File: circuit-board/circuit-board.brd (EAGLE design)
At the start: 100 x 80 mm, 51 parts, among them IC1 UA78M05DCY, Q1 BC547B, Q2 BC547B, U1 MAX3232, U2 ATMEGA328P_TQFP, U3 ADUM1201BRZ, Y2 16MHz

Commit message: Lay out circuit board, preliminary
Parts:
- removed 12V-IN-GPS: JST-XH-02-PIN-LONG-PAD, Rembrandt Electronics - JST XH Connectors v1-0:JST-XH-02-PACKAGE-LONG-PAD
- added 12V-IN: JST-XH-02-PIN-LONG-PAD, Rembrandt Electronics - JST XH Connectors v1-0:JST-XH-02-PACKAGE-LONG-PAD
- moved R10 74.6 mm to (39.4, 14.0), turned to 270 degrees
- moved Q2 51.3 mm to (44.5, 38.1)
- moved OK1 48.6 mm to (30.5, 11.4), turned to 270 degrees
- moved C5 45.1 mm to (35.6, 17.8), turned to 180 degrees
- moved C12 43.3 mm to (2.54, 5.08)
- moved EXP-GND 43.1 mm to (54.6, 38.1)
- moved EXT-GND 43.1 mm to (57.1, 38.1)
- moved HANDSET 43.1 mm to (50.8, 45.7)
- moved Y2 40.6 mm to (2.54, 8.89), turned to 270 degrees
- moved UC-DBG 40.4 mm to (5.08, 2.54), turned to 180 degrees
- moved MIC-XFMR 39.9 mm to (34.3, 27.9)
- moved C1 39.6 mm to (31.8, 38.1), turned to 90 degrees
- moved C13 38.6 mm to (2.54, 12.7), turned to 180 degrees
- moved SPK-SW 38.3 mm to (55.9, 14.0), turned to 0 degrees
- moved R1 38.1 mm to (58.4, 10.2)
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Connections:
- net 12V: now also 12V-IN.2; no longer 12V-IN-GPS.2
- net GNDA: now also 12V-IN.1; no longer 12V-IN-GPS.1
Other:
- board size 100 x 80 mm -> 61 x 50.8 mm

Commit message: Minimize V2 board layout
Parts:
- moved ICSP 33.5 mm to (2.03, 37.0)
- moved UC-DBG 23.6 mm to (2.03, 25.9), turned to 270 degrees
- moved R3 20.7 mm to (32.1, 7.62)
- moved UC-SS 16.0 mm to (14.5, 18.3), turned to 0 degrees
- moved 12V-IN 16.0 mm to (14.7, 34.3)
- moved FB1 14.9 mm to (10.5, 30.6)
- moved R6 14.7 mm to (14.0, 30.6)
- moved C18 14.5 mm to (17.4, 30.6)
- moved Q2 11.1 mm to (33.8, 35.2)
- moved C9 10.5 mm to (36.7, 9.27)
- moved R1 10.5 mm to (48.3, 7.49), turned to 180 degrees
- moved EXP-GND 10.5 mm to (44.6, 35.1)
- moved EXT-GND 10.5 mm to (47.1, 35.1)
- moved R7 10.4 mm to (26.7, 38.2)
- moved SPK-XFMR 10.3 mm to (42.0, 25.4)
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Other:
- board size 61 x 50.8 mm -> 50.8 x 45.7 mm

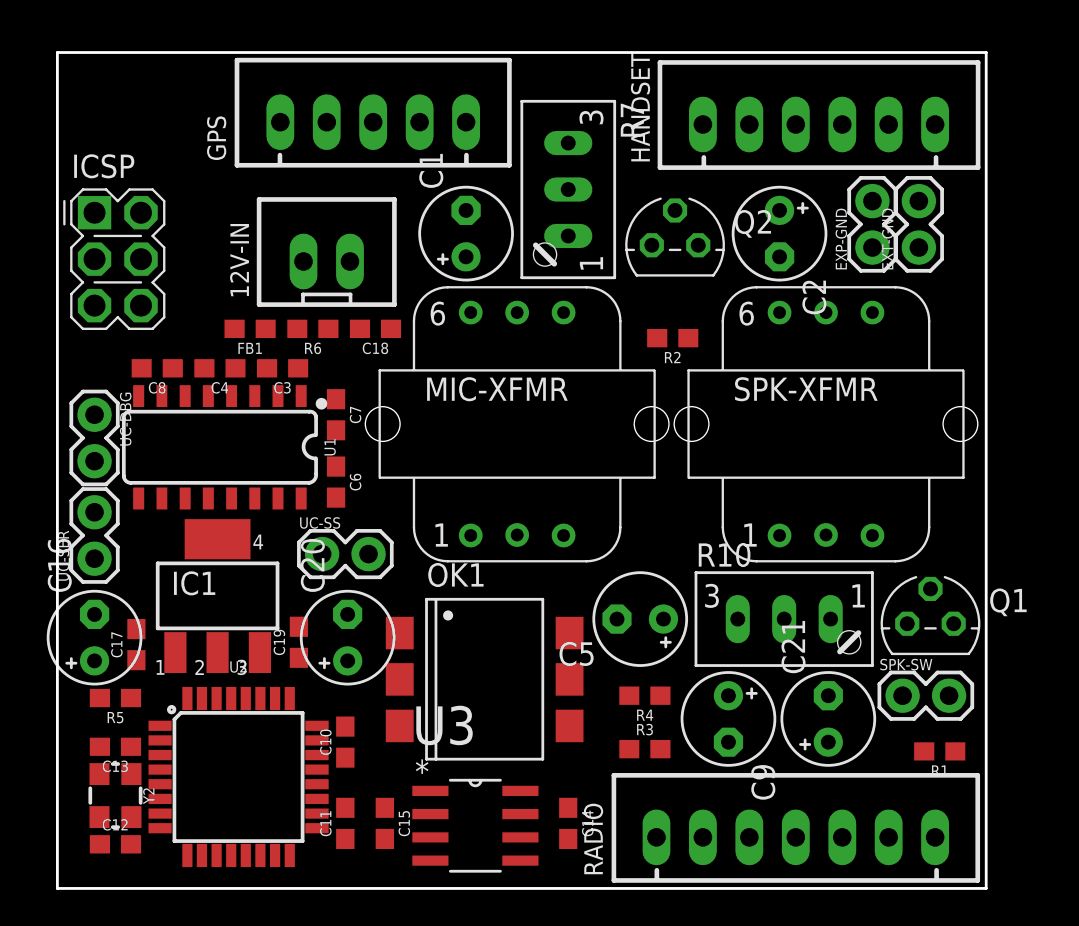
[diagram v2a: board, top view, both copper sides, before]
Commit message: Add ground planes, routes to V2 board
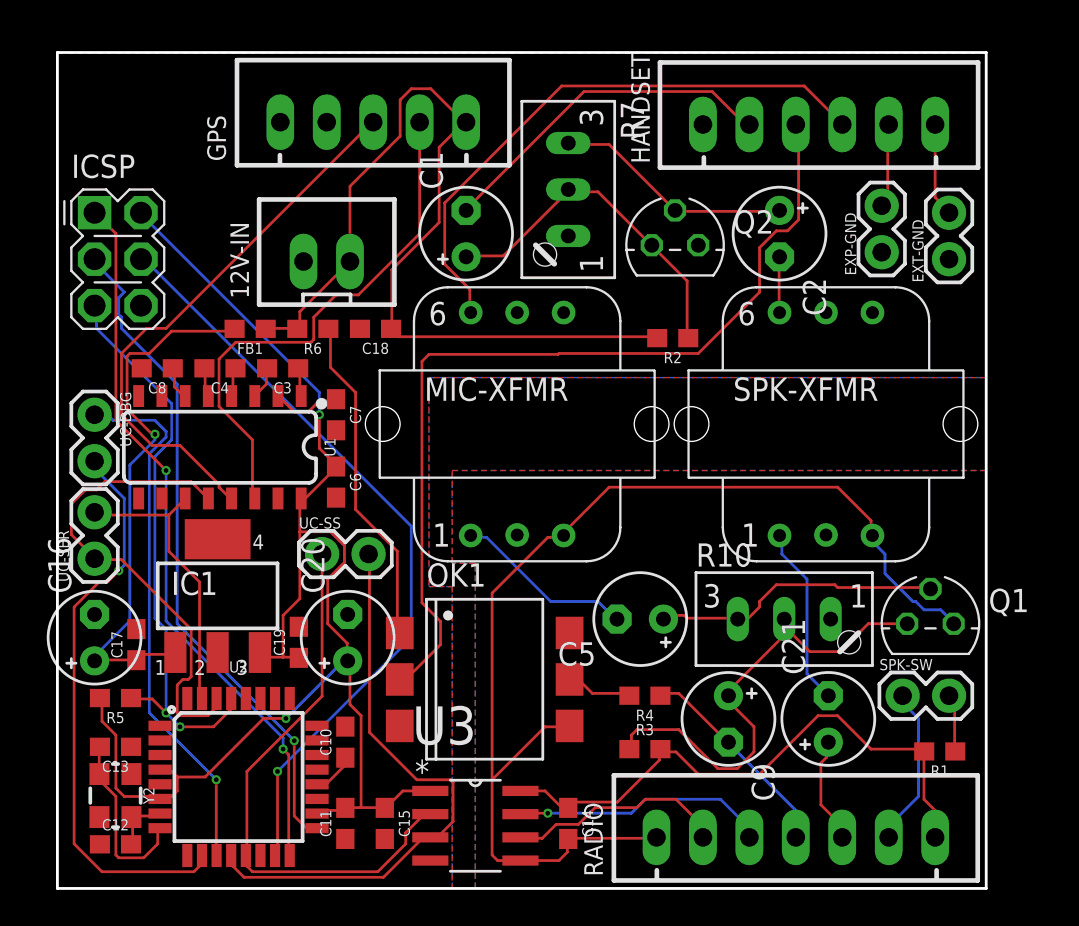
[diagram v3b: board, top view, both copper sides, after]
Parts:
- R10, R7: value (none) -> 100k
- moved EXT-GND 1.77 mm to (48.8, 34.4)
- moved EXP-GND 0.57 mm to (45.1, 34.8)
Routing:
- net +5V: track 0.00 -> 80.5 mm, vias 0 -> 2
- net GND: track 0.00 -> 62.1 mm
- net HANDSET-PTT: track 0.00 -> 49.9 mm
- net 12V: track 0.00 -> 49.1 mm
- net UC-MOSI: track 0.00 -> 42.1 mm, vias 0 -> 1
- net UC-MISO: track 0.00 -> 39.6 mm, vias 0 -> 2
- net UC-SCK: track 0.00 -> 36.8 mm, vias 0 -> 1
- net 3.3V: track 0.00 -> 32.0 mm
- net HANDSET-MIC: track 0.00 -> 31.9 mm
- net UC-SS-TX: track 0.00 -> 31.8 mm
- net UC-RESET: track 0.00 -> 31.8 mm, vias 0 -> 2
- net UC-DBG-TX: track 0.00 -> 31.3 mm, vias 0 -> 1
- net UC-SS-RX: track 0.00 -> 30.6 mm
- net GPS-TX: track 0.00 -> 30.4 mm
- net N$1: track 0.00 -> 29.9 mm, vias 0 -> 1
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- added copper zone on layer 1, net GND
- added copper zone on layer 16, net GND
- added copper zone on layer 1, net GNDA
- added copper zone on layer 16, net GNDA

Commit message: Route V2 board manually, fix up silkscreen
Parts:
- U2: value ATMEGA328P_TQFP -> ATMEGA328P
- moved ICSP 33.9 mm to (11.9, 4.57), turned to 270 degrees
- moved C16 28.0 mm to (4.32, 41.7), turned to 0 degrees
- moved C17 25.8 mm to (3.94, 39.1), turned to 0 degrees
- moved UC-DBG 24.0 mm to (3.94, 2.03), turned to 180 degrees
- moved C19 19.3 mm to (3.56, 30.2), turned to 0 degrees
- moved IC1 18.8 mm to (6.22, 34.7), turned to 270 degrees
- moved C20 17.6 mm to (5.08, 27.6), turned to 0 degrees
- moved UC-SS 13.7 mm to (15.4, 4.57), turned to 270 degrees
- moved C12 8.53 mm to (2.54, 10.9)
- moved C11 6.60 mm to (15.7, 10.2)
- moved C10 5.59 mm to (15.7, 13.6)
- moved U2 5.59 mm to (9.91, 11.7)
- moved C6 3.91 mm to (16.1, 18.4)
- moved C7 3.91 mm to (16.1, 22.1)
- moved C3 3.91 mm to (13.2, 24.6)
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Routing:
- net GND: track 62.1 -> 0.00 mm
- net UC-MISO: track 39.6 -> 3.14 mm, vias 2 -> 0
- net UC-MOSI: track 42.1 -> 6.40 mm, vias 1 -> 0
- net UC-SCK: track 36.8 -> 14.2 mm
- net UC-DBG-TX: track 31.3 -> 8.99 mm, vias 1 -> 0
- net UC-DBG-RX: track 29.4 -> 7.97 mm, vias 1 -> 0
- net N$1: track 29.9 -> 13.9 mm, vias 1 -> 0
- net UC-RX: track 26.7 -> 11.7 mm, vias 0 -> 1
- net UC-SS-RX: track 30.6 -> 17.9 mm, vias 0 -> 1
- net 12V: track 49.1 -> 36.3 mm
- net UC-RESET: track 31.8 -> 21.1 mm
- net UC-SS-TX: track 31.8 -> 21.7 mm, vias 0 -> 1
- net UC-TX: track 16.2 -> 7.75 mm
- net HANDSET-MIC: track 31.9 -> 26.1 mm, vias 0 -> 1
- net N$3: track 26.9 -> 22.2 mm
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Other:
- board text added: "12V"
- board text added: "3.3V"
- board text added: "EXP"
- board text added: "EXT"
- board text added: "GND"
- board text added: "Garmin + VX-8DR + Handset/Mic Adapter github.com/paulmandal/radio-adapter v2.0"
- board text added: "MIC"
- board text added: "MIC/PTT"
- board text added: "PTT"
- board text added: "RX"
- board text added: "S-GND"
- board text added: "SPK"
- board text added: "SPK-SEL"
- board text added: "TX"

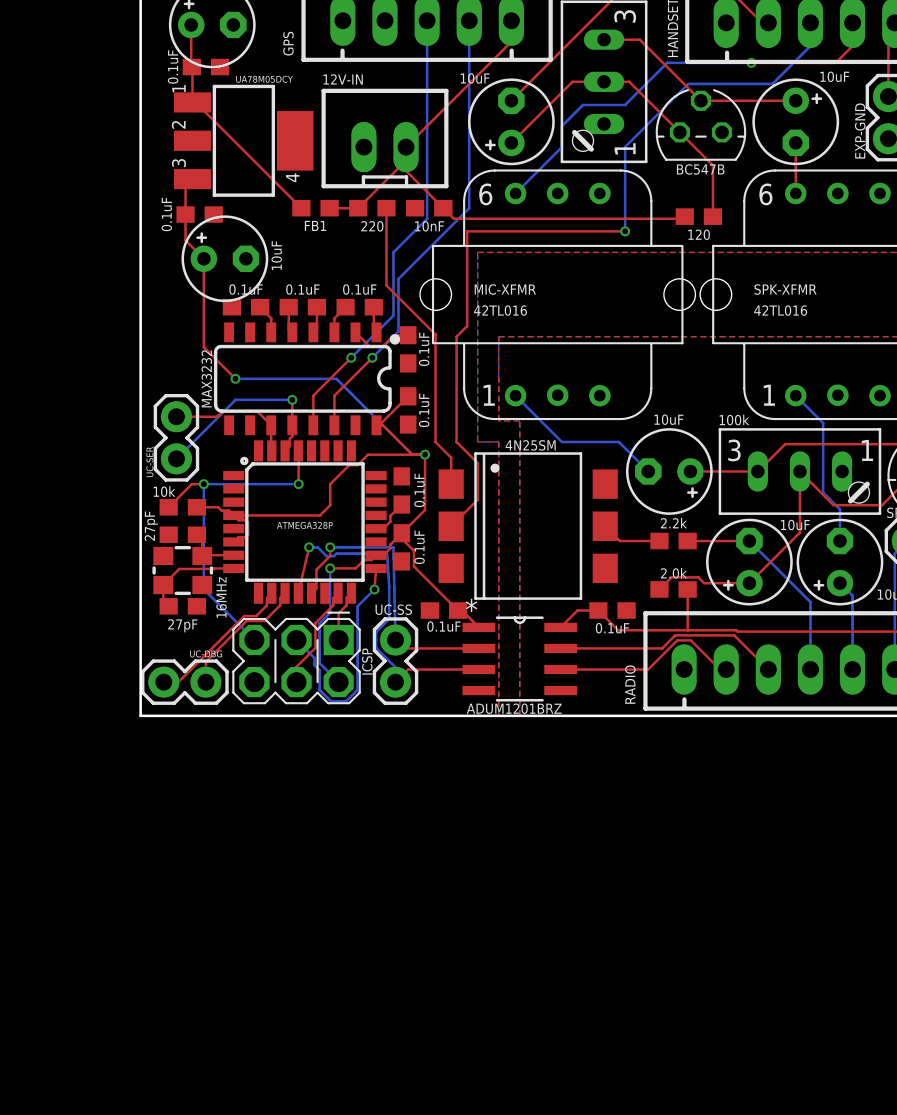
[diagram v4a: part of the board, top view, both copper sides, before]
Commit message: Tweak some resistor values in V2 board based on breadboard testing.  Add small input resistors on both amplifying transistors -- this cleans up the mic signal a lot!
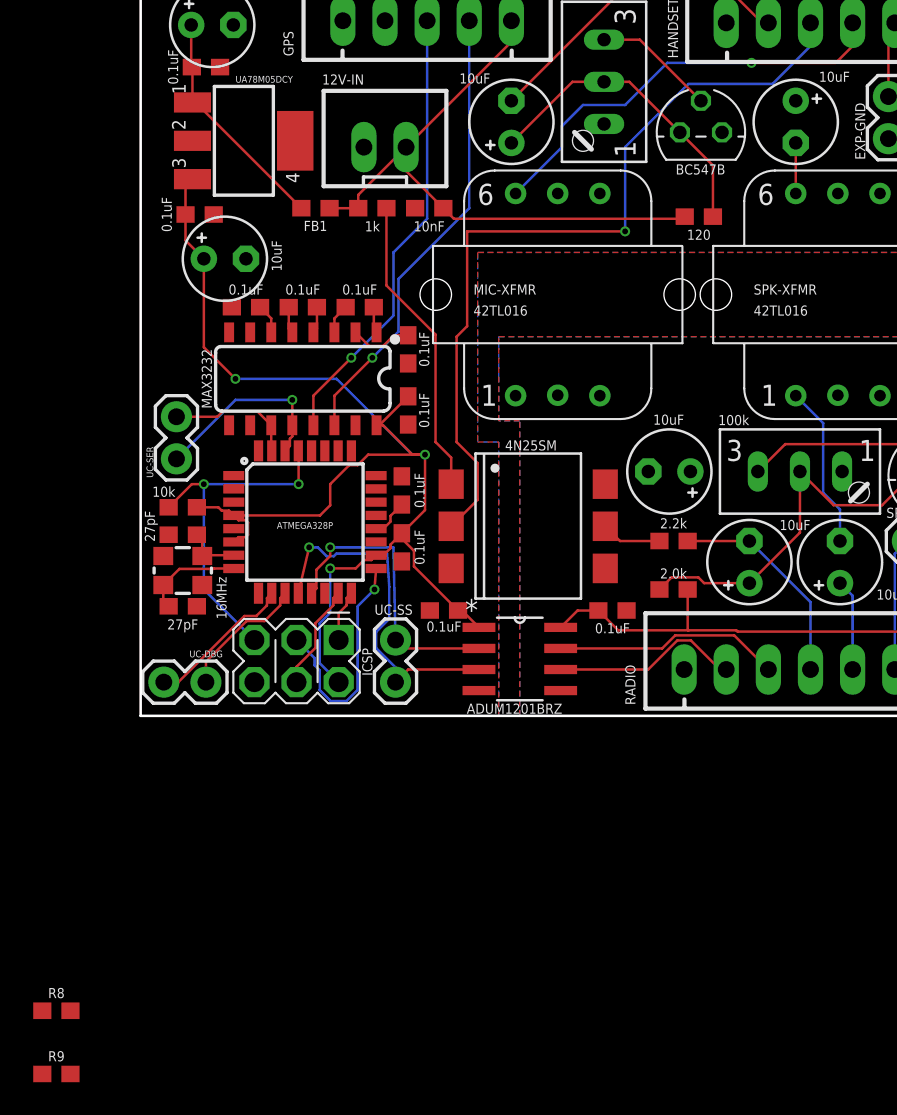
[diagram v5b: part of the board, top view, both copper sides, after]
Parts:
- added R8, R9: 100, SparkFun-Resistors:0603
- R6: value 220 -> 1k
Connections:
- new net N$10: C2.+, R9.1
- new net N$8: C5.+, R8.1
- net N$4: now also R8.2; no longer C5.+
- net N$5: now also R9.2; no longer C2.+
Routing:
- net N$7: track 9.89 -> 0.00 mm
- net N$5: track 13.1 -> 7.37 mm
- net N$4: track 15.3 -> 11.2 mm
- net 12V: track 36.3 -> 37.1 mm
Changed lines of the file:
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@@
 <attribute name="VALUE" x="1.397" y="13.208" size="0.6096" layer="25" font="vector" ratio="20" rot="R180" align="top-center"/>
-</element>
-<element name="R6" library="SparkFun-Resistors" library_urn="urn:adsk.eagle:library:532" package="0603" package3d_urn="urn:adsk.eagle:package:39650/1" value="220" x="13.97" y="30.607" smashed="yes" rot="R180">
-<attribute name="PROD_ID" value="RES-07861" x="13.97" y="30.607" size="1.778" layer="27" rot="R180" display="off"/>
-<attribute name="VALUE" x="13.97" y="29.21" size="0.6096" layer="25" font="vector" ratio="20" rot="R180" align="top-center"/>
 </element>
 <element name="RADIO" library="Rembrandt Electronics - JST XH Connectors v1-0" package="JST-XH-07-PACKAGE-LONG-PAD" value="JST-XH-07-PIN-LONG-PAD" x="40.386" y="2.794" smashed="yes">
@@
 <element name="R7" library="pot" library_urn="urn:adsk.eagle:library:331" package="S64W" package3d_urn="urn:adsk.eagle:package:22708/1" value="100k" x="26.67" y="38.227" smashed="yes" rot="R270">
 <attribute name="VALUE" x="25.4254" y="43.307" size="0.6096" layer="25" ratio="10"/>
+</element>
+<element name="R6" library="SparkFun-Resistors" library_urn="urn:adsk.eagle:library:532" package="0603" package3d_urn="urn:adsk.eagle:package:39650/1" value="1k" x="13.97" y="30.607" smashed="yes" rot="R180">
+<attribute name="PROD_ID" value="RES-07856" x="13.97" y="30.607" size="1.778" layer="27" rot="R180" display="off"/>
+<attribute name="VALUE" x="13.97" y="29.21" size="0.6096" layer="25" font="vector" ratio="20" rot="R180" align="top-center"/>
+</element>
+<element name="R8" library="SparkFun-Resistors" library_urn="urn:adsk.eagle:library:532" package="0603" package3d_urn="urn:adsk.eagle:package:39650/1" value="100" x="-5.08" y="-17.78">
+<attribute name="PROD_ID" value="RES-07863" x="-5.08" y="-17.78" size="1.778" layer="27" display="off"/>
+</element>
+<element name="R9" library="SparkFun-Resistors" library_urn="urn:adsk.eagle:library:532" package="0603" package3d_urn="urn:adsk.eagle:package:39650/1" value="100" x="-5.08" y="-21.59">
+<attribute name="PROD_ID" value="RES-07863" x="-5.08" y="-21.59" size="1.778" layer="27" display="off"/>
 </element>
 </elements>
@@
 <contactref element="FB1" pad="1"/>
 <contactref element="R2" pad="2"/>
-<contactref element="R6" pad="2"/>
-<wire x1="11.391" y1="30.607" x2="13.12" y2="30.607" width="0.1524" layer="1"/>
 <wire x1="18.249" y1="30.607" x2="16.002" y2="32.854" width="0.1524" layer="1"/>
 <wire x1="16.002" y1="32.854" x2="16.002" y2="34.29" width="0.1524" layer="1"/>
@@
 <wire x1="16.002" y1="34.29" x2="22.352" y2="40.64" width="0.1524" layer="1"/>
 <wire x1="22.352" y1="40.64" x2="22.352" y2="41.91" width="0.1524" layer="1"/>
-<wire x1="13.12" y1="30.607" x2="16.002" y2="33.489" width="0.1524" layer="1"/>
 <wire x1="16.002" y1="33.489" x2="16.002" y2="34.29" width="0.1524" layer="1"/>
+<contactref element="R6" pad="2"/>
+<wire x1="16.002" y1="34.29" x2="13.12" y2="31.408" width="0.1524" layer="1"/>
+<wire x1="13.12" y1="31.408" x2="13.12" y2="30.607" width="0.1524" layer="1"/>
+<wire x1="13.12" y1="30.607" x2="11.391" y2="30.607" width="0.1524" layer="1"/>
 </signal>
 <signal name="HANDSET-SPK">
@@
 <signal name="N$4">
 <contactref element="Q1" pad="2"/>
-<contactref element="C5" pad="+"/>
 <contactref element="R10" pad="E"/>
 <wire x1="47.752" y1="16.383" x2="38.862" y2="16.383" width="0.1524" layer="1"/>
 <wire x1="38.862" y1="16.383" x2="37.211" y2="14.732" width="0.1524" layer="1"/>
-<wire x1="37.211" y1="14.732" x2="33.147" y2="14.732" width="0.1524" layer="1"/>
+<contactref element="R8" pad="2"/>
+<wire x1="-4.23" y1="-17.78" x2="37.211" y2="14.732" width="0" layer="19" extent="1-1"/>
 </signal>
 <signal name="+5V">
@@
 <signal name="N$5">
 <contactref element="Q2" pad="2"/>
-<contactref element="C2" pad="+"/>
 <contactref element="R7" pad="E"/>
 <wire x1="33.782" y1="37.084" x2="30.099" y2="40.767" width="0.1524" layer="1"/>
 <wire x1="30.099" y1="40.767" x2="27.94" y2="40.767" width="0.1524" layer="1"/>
-<wire x1="39.497" y1="37.084" x2="33.782" y2="37.084" width="0.1524" layer="1"/>
+<contactref element="R9" pad="2"/>
+<wire x1="-4.23" y1="-21.59" x2="33.782" y2="37.084" width="0" layer="19" extent="1-1"/>
 </signal>
 <signal name="N$6">
@@
 <wire x1="41.148" y1="13.462" x2="41.148" y2="17.653" width="0.1524" layer="16"/>
 </signal>
-<signal name="N$7">
-<contactref element="C5" pad="-"/>
-<contactref element="MIC-XFMR" pad="1"/>
-<wire x1="30.607" y1="14.732" x2="28.829" y2="16.51" width="0.1524" layer="16"/>
-<wire x1="28.829" y1="16.51" x2="25.4" y2="16.51" width="0.1524" layer="16"/>
-<wire x1="25.4" y1="16.51" x2="22.606" y2="19.304" width="0.1524" layer="16"/>
-</signal>
 <signal name="N$9">
 <contactref element="OK1" pad="1"/>
-<contactref element="R6" pad="1"/>
 <wire x1="18.723" y1="13.97" x2="18.723" y2="15.567" width="0.1524" layer="1"/>
 <wire x1="18.723" y1="15.567" x2="17.78" y2="16.51" width="0.1524" layer="1"/>
 <wire x1="17.78" y1="16.51" x2="17.78" y2="22.987" width="0.1524" layer="1"/>
-<wire x1="14.82" y1="25.947" x2="14.82" y2="30.607" width="0.1524" layer="1"/>
-<wire x1="17.78" y1="22.987" x2="14.82" y2="25.947" width="0.1524" layer="1"/>
+<wire x1="14.82" y1="25.947" x2="17.78" y2="22.987" width="0.1524" layer="1"/>
+<contactref element="R6" pad="1"/>
+<wire x1="14.82" y1="30.607" x2="14.82" y2="25.947" width="0.1524" layer="1"/>
 </signal>
 <signal name="RADIO-PTT-SENSE">
@@
 <wire x1="28.902" y1="10.541" x2="31.281" y2="10.541" width="0.1524" layer="1"/>
 </signal>
+<signal name="N$7">
+<contactref element="MIC-XFMR" pad="1"/>
+<contactref element="C5" pad="-"/>
+<wire x1="22.606" y1="19.304" x2="30.607" y2="14.732" width="0" layer="19" extent="1-1"/>
+</signal>
+<signal name="N$8">
+<contactref element="C5" pad="+"/>
+<contactref element="R8" pad="1"/>
+<wire x1="-5.93" y1="-17.78" x2="33.147" y2="14.732" width="0" layer="19" extent="1-1"/>
+</signal>
+<signal name="N$10">
+<contactref element="C2" pad="+"/>
+<contactref element="R9" pad="1"/>
+<wire x1="-5.93" y1="-21.59" x2="39.497" y2="37.084" width="0" layer="19" extent="1-1"/>
+</signal>
 </signals>
